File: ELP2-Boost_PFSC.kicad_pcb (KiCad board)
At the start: 2 copper layers, 43 parts, among them J1 Screw_Terminal_01x03, J2 Screw_Terminal_01x03, Q1 12n50C3, U1 UCC38050

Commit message: Changes:  - Added netclasses  - Better footprint for testpoints  - EMI filter
TODO:
 - Route the rest of the board
 - Different versions of the board to make sure its approved on monday
 - Get shunt footprint
 - Figure out wich connections can be jumpered
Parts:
- TP1, TP2, TP3: footprint TestPoint:TestPoint_Pad_1.0x1.0mm -> TestPoint:TestPoint_THTPad_2.5x2.5mm_Drill1.2mm; moved to F.Cu
- moved D6 104.7 mm to (94.4, 91.2), turned to 0 degrees
- moved Q1 101.1 mm to (105.0, 91.2), turned to 0 degrees
- moved J1 98.6 mm to (46.0, 165.5), turned to 0 degrees
- moved R4 97.0 mm to (88.5, 113.5), turned to 0 degrees
- moved F1 96.5 mm to (67.5, 165.5), turned to 90 degrees
- moved R7 91.0 mm to (88.5, 125.6), turned to 0 degrees
- moved HS1 90.0 mm to (108.7, 44.5), turned to 0 degrees
- moved R6 84.5 mm to (88.5, 121.6), turned to 0 degrees
- moved J2 84.3 mm to (136.3, 164.9), turned to 0 degrees
- moved R10 74.9 mm to (88.5, 133.7), turned to 0 degrees
- moved D2 69.4 mm to (108.6, 112.2), turned to 0 degrees
- moved R5 66.2 mm to (88.5, 117.5)
- moved C8 63.9 mm to (122.7, 91.5), turned to 0 degrees
- moved D5 63.7 mm to (58.0, 74.1)
- moved C3 63.1 mm to (102.2, 109.4), turned to 0 degrees
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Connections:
- net /PFC/CS_L renamed /PFC/Current_Sense
- net /PFC/ZCD_L renamed /PFC/Zero_Cross
- FL1 pad 1: Net-(CX1-Pad1) -> /Prot-EMI/N
- FL1 pad 2: /Prot-EMI/P' -> /Prot-EMI/N'
- FL1 pad 3: /Prot-EMI/N -> Net-(CX1-Pad1)
- FL1 pad 4: /Prot-EMI/N' -> /Prot-EMI/P'
- J1 pad 1: /Prot-EMI/P -> /Prot-EMI/N
- J1 pad 3: /Prot-EMI/N -> /Prot-EMI/P
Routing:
- net Earth: track 262.0 -> 0.00 mm
- net Net-(D6-A): track 81.0 -> 0.00 mm
- net /Vcc: track 55.7 -> 0.00 mm
- net /PFC/Mult_In: track 53.7 -> 0.00 mm
- net Net-(D5-+): track 51.6 -> 0.00 mm
- net /PFC/Multin: track 41.9 -> 0.00 mm
- net /ZCD: track 41.2 -> 0.00 mm
- net /PWM: track 39.8 -> 0.00 mm
- net /PFC/VO_SNS: track 33.9 -> 0.00 mm
- net /PFC/Comp: track 32.1 -> 0.00 mm
- net /Out+: track 23.9 -> 0.00 mm
- net Net-(R6-Pad2): track 22.6 -> 0.00 mm
- net Net-(R12-Pad2): track 17.6 -> 0.00 mm
- net Net-(D7-K): track 16.7 -> 0.00 mm
- net /Prot-EMI/N': track 28.9 -> 45.6 mm
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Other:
- board outline added: 130 x 150 mm

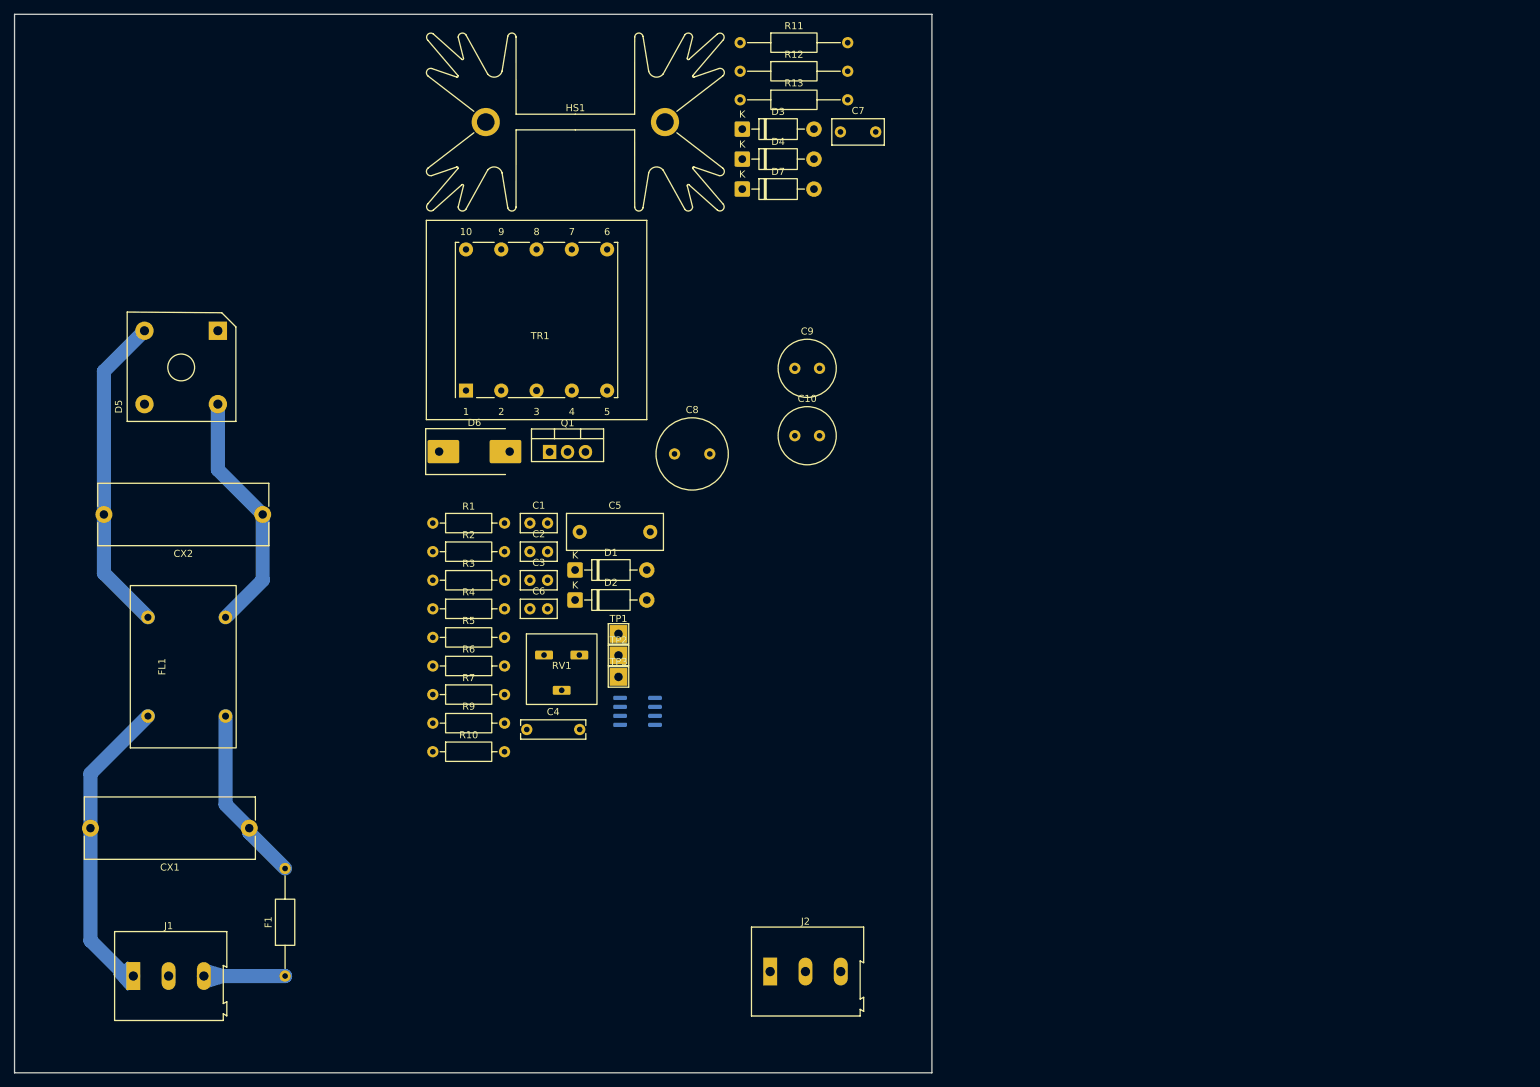
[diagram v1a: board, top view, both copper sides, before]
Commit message: Changes:  - Grouped blocks of components for labeling/testing  - Labeled Test conditions on board Todo:  - Arange blocks into a more sensible shape  - Connect them
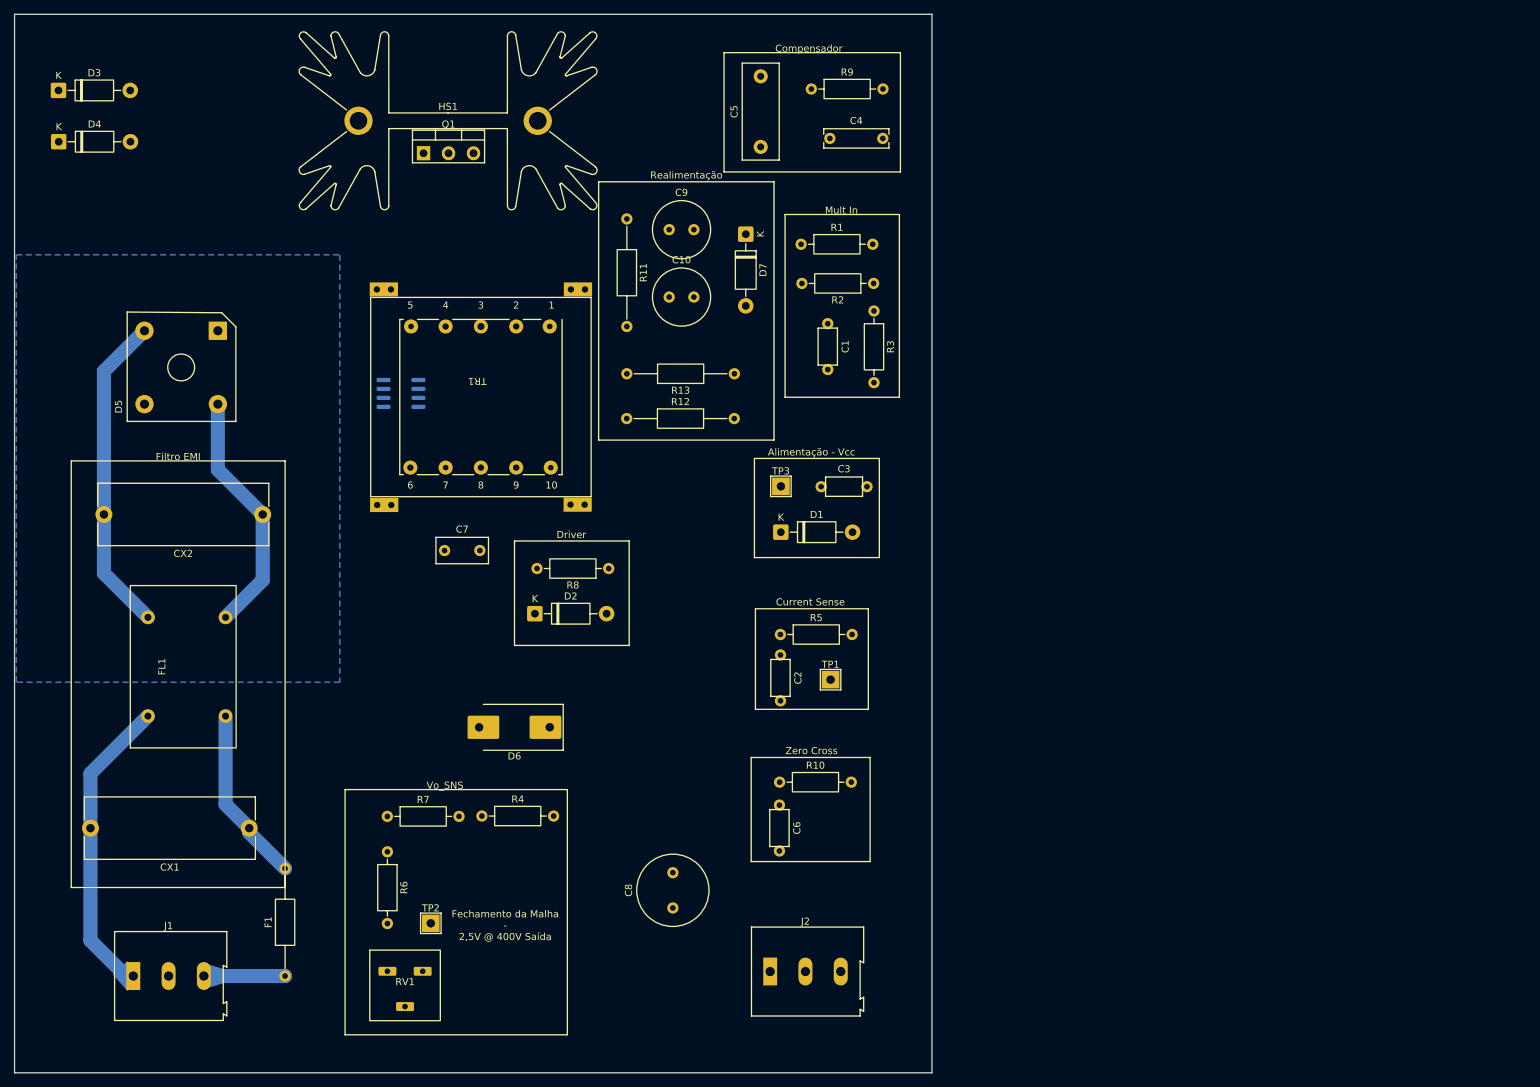
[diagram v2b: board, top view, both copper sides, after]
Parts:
- added R8: 10, Resistor_THT:R_Axial_DIN0207_L6.3mm_D2.5mm_P10.16mm_Horizontal, F.Cu at (113.4, 107.8)
- moved R9 104.6 mm to (142.1, 39.8)
- moved D3 97.0 mm to (35.4, 40.0)
- moved D4 96.9 mm to (35.5, 47.3)
- moved C4 94.1 mm to (144.8, 46.8)
- moved C7 81.6 mm to (90.2, 105.2)
- moved R3 73.2 mm to (151.0, 71.2), turned to -90 degrees
- moved R2 73.1 mm to (150.9, 67.3), turned to 180 degrees
- moved R1 65.5 mm to (140.7, 61.8)
- moved C8 64.3 mm to (122.5, 155.8), turned to 90 degrees
- moved C5 60.3 mm to (134.9, 48.0), turned to 90 degrees
- moved U1 56.2 mm to (84.0, 82.9)
- moved R12 51.8 mm to (116.0, 86.5)
- moved RV1 50.0 mm to (84.5, 166.8)
- moved C1 49.7 mm to (144.4, 75.0), turned to -90 degrees
- moved R10 49.3 mm to (137.6, 138.0)
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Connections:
- D2 pad 1: /PWM -> /PFC/Driver
- U1 pad 7: /PWM -> /PFC/Driver
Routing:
- added copper zone on B.Cu, net Earth
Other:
- board text added: "Alimentação - Vcc"
- board text added: "Compensador"
- board text added: "Current Sense"
- board text added: "Driver"
- board text added: "Fechamento da Malha - 2,5V @ 400V Saída"
- board text added: "Filtro EMI"
- board text added: "Mult In"
- board text added: "Realimentação"
- board text added: "Vo_SNS"
- board text added: "Zero Cross"

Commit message: Changed:  - Added basic routing/positioning  - Better netclasses  - Determined location for the IC TODO:  - Finish routing  - Add jumpers for voltage signals
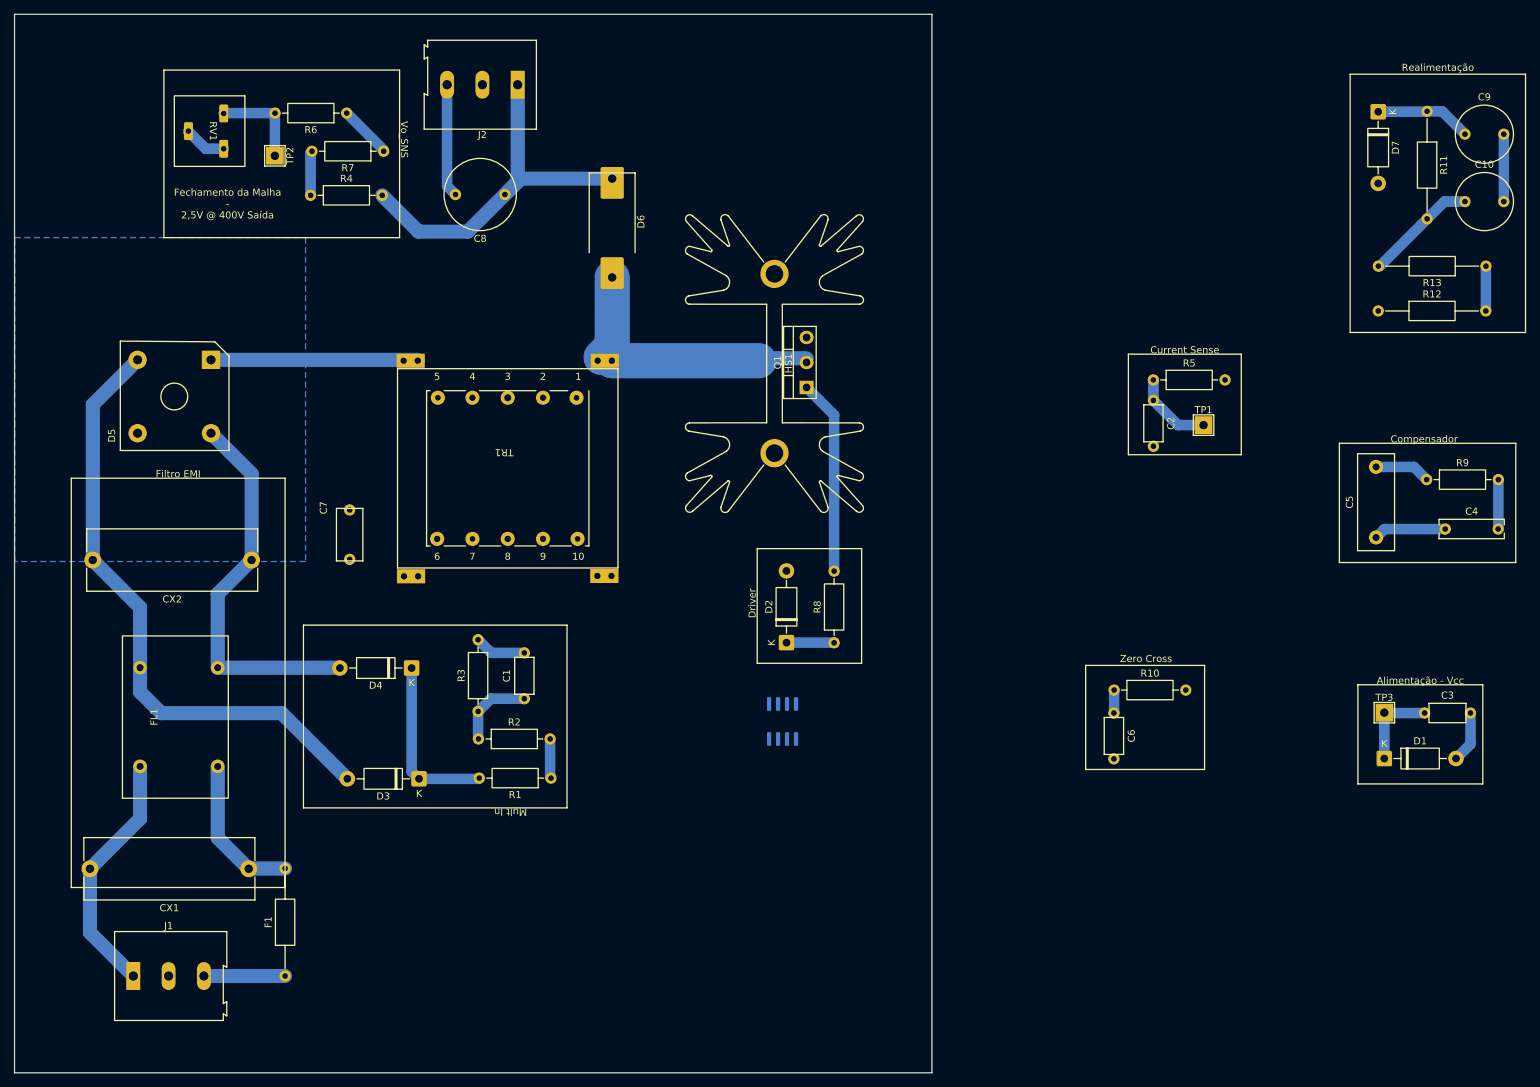
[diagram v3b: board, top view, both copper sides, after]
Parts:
- moved J2 130.7 mm to (100.5, 39.2), turned to 180 degrees
- moved RV1 124.2 mm to (56.9, 45.8), turned to -90 degrees
- moved C10 114.6 mm to (235.8, 55.8)
- moved C9 114.6 mm to (235.8, 46.2)
- moved R11 114.4 mm to (229.4, 43.0)
- moved TP2 111.0 mm to (66.1, 49.3), turned to -90 degrees
- moved D3 110.1 mm to (86.5, 137.6), turned to 180 degrees
- moved R12 107.6 mm to (222.5, 71.2)
- moved R13 107.6 mm to (237.7, 64.9)
- moved R6 104.8 mm to (76.3, 43.2), turned to 180 degrees
- moved C8 104.1 mm to (97.7, 54.8), turned to 180 degrees
- moved C5 103.3 mm to (222.2, 103.3)
- moved C4 103.3 mm to (231.9, 102.2)
- moved R9 103.3 mm to (229.3, 95.2)
- moved R7 94.3 mm to (81.5, 48.6), turned to 180 degrees
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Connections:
- TR1 pad 1: Net-(D5-+) -> Net-(D6-A)
- TR1 pad 5: Net-(D6-A) -> Net-(D5-+)
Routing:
- net Earth: track 0.00 -> 54.2 mm
- net /Out+: track 0.00 -> 54.1 mm
- net /Prot-EMI/N': track 45.6 -> 86.9 mm
- net Net-(D6-A): track 0.00 -> 39.7 mm
- net Net-(D5-+): track 0.00 -> 29.4 mm
- net /Vcc: track 0.00 -> 28.3 mm
- net /PWM: track 0.00 -> 27.6 mm
- net /PFC/Multin: track 0.00 -> 24.7 mm
- net /Prot-EMI/P': track 35.0 -> 54.9 mm
- net Net-(D7-K): track 0.00 -> 13.7 mm
- net Net-(R6-Pad2): track 0.00 -> 13.3 mm
- net /PFC/Current_Sense: track 0.00 -> 11.5 mm
- net /PFC/Mult_In: track 0.00 -> 11.2 mm
- net /PFC/Comp: track 0.00 -> 10.3 mm
- net /Prot-EMI/N: track 43.3 -> 35.2 mm
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
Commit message: Changes:  - Connected everything TODO:  - Redesign so that UCC is surrounded by the ground plane
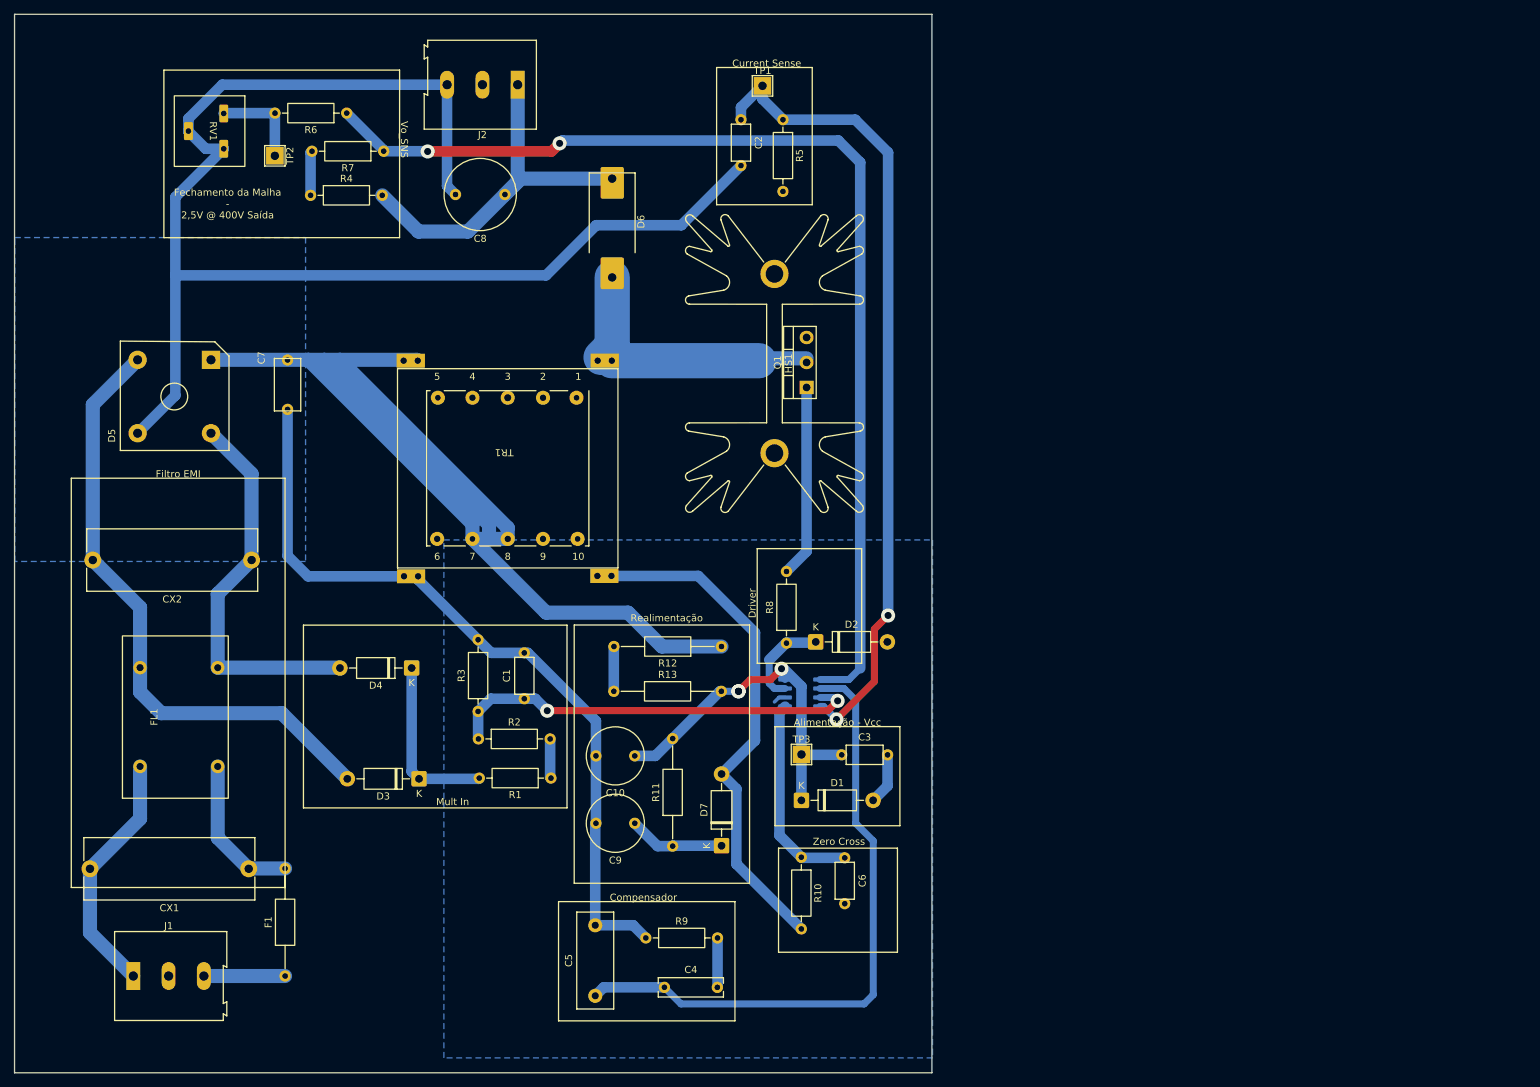
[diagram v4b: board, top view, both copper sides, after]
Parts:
- moved C9 154.4 mm to (116.1, 143.8), turned to 180 degrees
- moved R11 149.2 mm to (122.5, 147.1), turned to 90 degrees
- moved C10 143.1 mm to (116.1, 134.3), turned to 180 degrees
- moved D7 139.6 mm to (129.4, 147.0), turned to 90 degrees
- moved R13 137.5 mm to (114.1, 125.2), turned to 0 degrees
- moved C4 128.3 mm to (121.3, 167.1)
- moved C5 128.3 mm to (111.5, 168.3)
- moved R9 128.3 mm to (118.7, 160.1)
- moved R12 104.5 mm to (129.4, 118.8), turned to 180 degrees
- moved C3 82.8 mm to (148.4, 134.2)
- moved D1 82.8 mm to (140.7, 140.6)
- moved TP3 82.8 mm to (140.7, 134.1)
- moved TP1 78.9 mm to (135.2, 39.4)
- moved C2 70.7 mm to (132.2, 46.1)
- moved R5 64.1 mm to (138.1, 44.1), turned to -90 degrees
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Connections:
- TR1 pad 11: (no net) -> Net-(D5-+)
- TR1 pad 8: (no net) -> Net-(D5-+)
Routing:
- net Earth: track 54.2 -> 312.9 mm
- net Net-(D5-+): track 29.4 -> 181.2 mm
- net /PFC/VO_SNS: track 7.57 -> 155.1 mm, vias 0 -> 2
- net /PFC/Current_Sense: track 11.5 -> 115.4 mm, vias 0 -> 2
- net /PFC/Comp: track 10.3 -> 89.9 mm
- net /ZCD: track 0.00 -> 74.3 mm
- net /PFC/Mult_In: track 11.2 -> 59.6 mm, vias 0 -> 2
- net /PFC/Zero_Cross: track 3.26 -> 29.1 mm
- net /Vcc: track 28.3 -> 53.4 mm, vias 0 -> 3
- net /PFC/Driver: track 6.76 -> 13.5 mm
- net /PWM: track 27.6 -> 26.6 mm

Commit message: Changes:  - Added ground plane for analog components  - Better EMI shielding on UCC and MOSFET TODO:  - Try and get everything closer, somehow
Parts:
- moved TP2 16.4 mm to (81.3, 43.2)
- moved C3 13.3 mm to (140.4, 123.5)
- moved U1 4.23 mm to (141.1, 129.6)
- moved D1 4.23 mm to (140.9, 144.8)
- moved R10 4.23 mm to (140.9, 152.9)
- moved TP3 4.23 mm to (140.9, 138.3)
- moved C6 2.32 mm to (146.0, 152.9), turned to 0 degrees
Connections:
- TP2 pad 1: Net-(R6-Pad2) -> /PFC/VO_SNS
- TR1 pad 11: Net-(D5-+) -> (no net)
- TR1 pad 8: Net-(D5-+) -> (no net)
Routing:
- net /PFC/VO_SNS: track 155.1 -> 168.8 mm
- net /PFC/Comp: track 89.9 -> 76.2 mm
- net Earth: track 312.9 -> 322.7 mm, vias 0 -> 2
- net Net-(R6-Pad2): track 13.3 -> 7.32 mm
- net /Vcc: track 53.4 -> 49.0 mm, vias 3 -> 2
- net /ZCD: track 74.3 -> 78.6 mm
- net /PFC/Current_Sense: track 115.4 -> 119.5 mm
- net /PFC/Zero_Cross: track 29.1 -> 25.5 mm
- net /PFC/Driver: track 13.5 -> 17.1 mm
- net /PFC/Mult_In: track 59.6 -> 61.7 mm
